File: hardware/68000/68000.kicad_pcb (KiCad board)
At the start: 2 copper layers, 99.1 x 99.1 mm, 6 parts, among them J1 nuMezzanine_4x34, U1 MC68000P

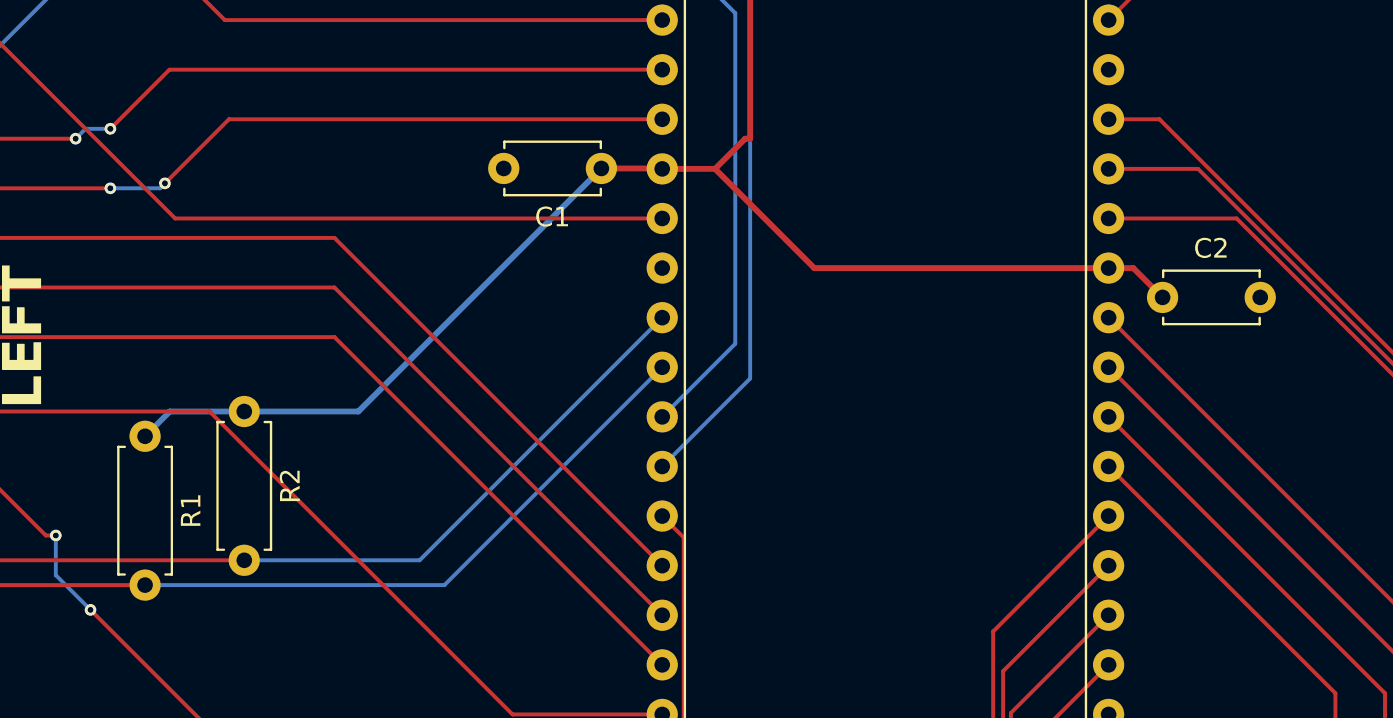
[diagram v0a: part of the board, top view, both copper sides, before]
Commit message: Update mainboard to revision 2
Add an additional 8 bidirectional channels
Replace SPI PSRAM with hyperram
Remove LEDs
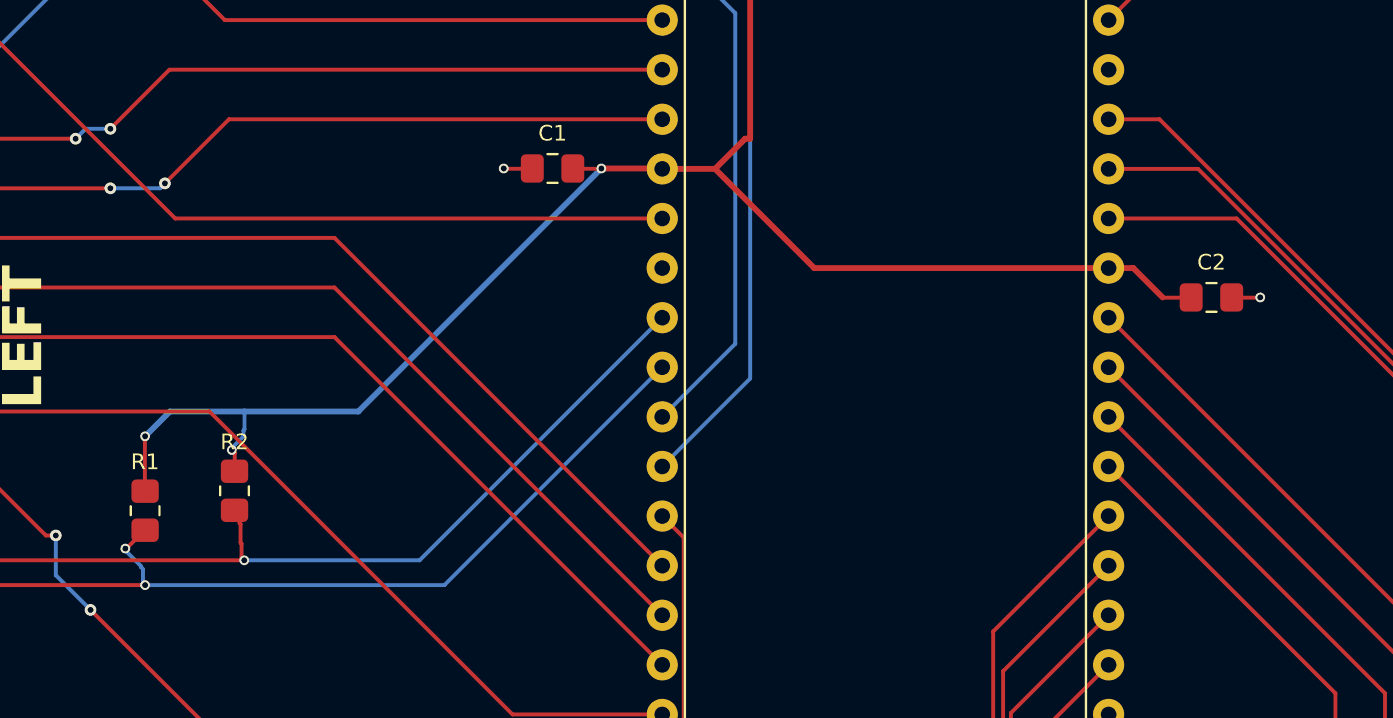
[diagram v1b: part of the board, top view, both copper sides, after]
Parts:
- C1, C2: footprint Capacitor_THT:C_Disc_D4.7mm_W2.5mm_P5.00mm -> Capacitor_SMD:C_0805_2012Metric_Pad1.18x1.45mm_HandSolder
- R1, R2: footprint Resistor_THT:R_Axial_DIN0207_L6.3mm_D2.5mm_P7.62mm_Horizontal -> Resistor_SMD:R_0805_2012Metric_Pad1.20x1.40mm_HandSolder
- moved R2 4.09 mm to (118.7, 105.1)
- moved R1 3.81 mm to (114.2, 106.2)
- moved C1 2.50 mm to (135.0, 88.6)
- moved C2 2.50 mm to (168.8, 95.2)
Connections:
- net /BX renamed /BX1
- net /BY renamed /BX2
- net /LX renamed /LX1
- net /LY renamed /LX2
- net /RX renamed /RX1
- net /RY renamed /RX2
- net /TX renamed /TX1
- net /TY renamed /TX2
- J1 pad 10: GND -> unconnected-(J1A-TX3-Pad10)
- J1 pad 102: unconnected-(J1E-NC-Pad102) -> GND
- J1 pad 112: GND -> unconnected-(J1B-LX3-Pad112)
- J1 pad 115: GND -> unconnected-(J1B-LX0-Pad115)
- J1 pad 13: GND -> unconnected-(J1A-TX0-Pad13)
- J1 pad 136: unconnected-(J1E-NC-Pad136) -> GND
- J1 pad 44: GND -> unconnected-(J1D-RX3-Pad44)
- J1 pad 47: GND -> unconnected-(J1D-RX0-Pad47)
- J1 pad 78: GND -> unconnected-(J1C-BX3-Pad78)
- J1 pad 81: GND -> unconnected-(J1C-BX0-Pad81)
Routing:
- net VCC: track 121.6 -> 130.9 mm, vias 0 -> 3
- net /LX2: track 41.3 -> 45.0 mm, vias 0 -> 2
- net GND: track 0.00 -> 2.98 mm, vias 0 -> 2
- net /LX1: track 42.3 -> 45.1 mm, vias 0 -> 1
